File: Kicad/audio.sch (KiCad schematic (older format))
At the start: 33 parts, among them J15 AudioJack3, J16 AudioJack2, J17 AudioJack3, J18 AudioJack3, U15 TLV320AIC23BPW, Y3 12 MHz

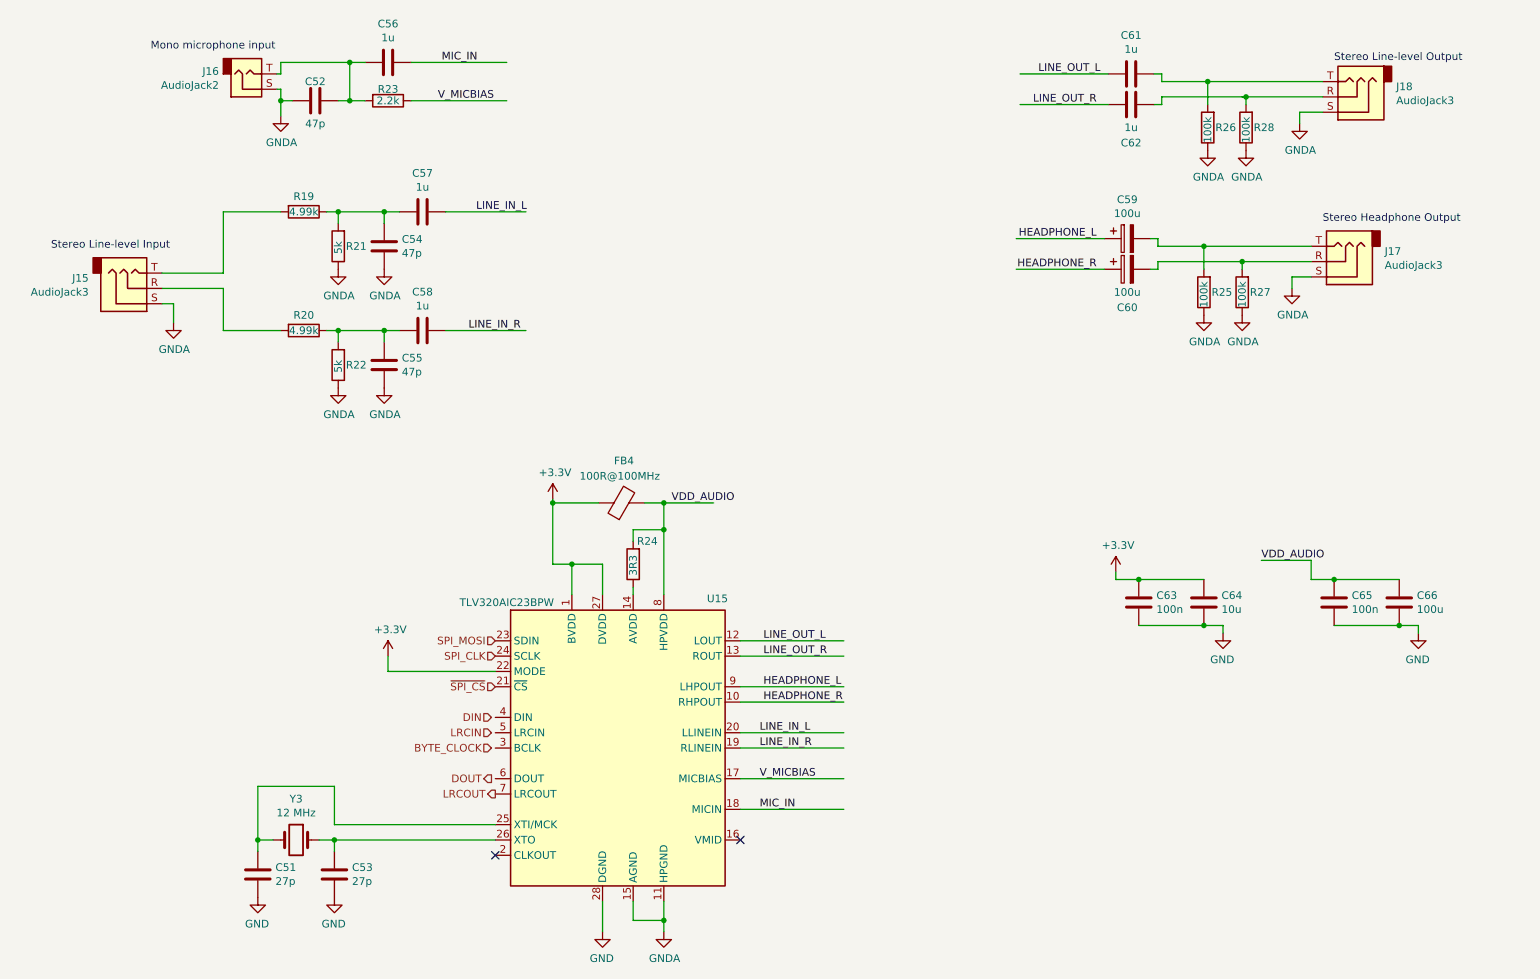
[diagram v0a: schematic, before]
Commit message: Removed USB FS hub. Added stacked USB A connector.
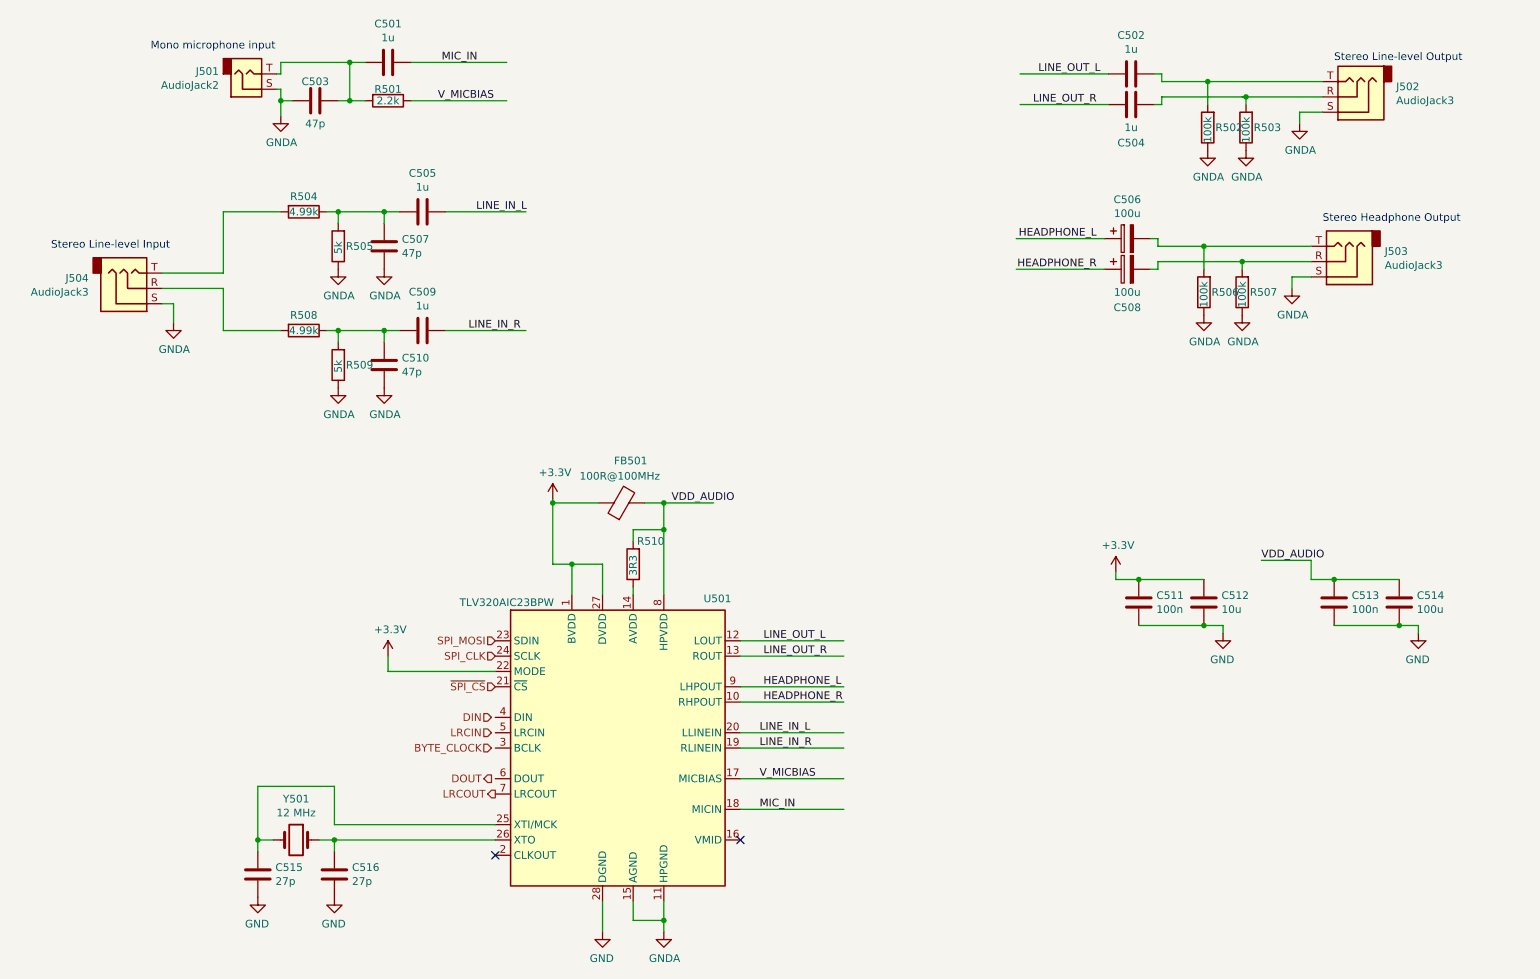
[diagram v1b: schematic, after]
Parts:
- C503: renamed from C52; footprint (none) -> Capacitor_SMD:C_0402_1005Metric
- C507: renamed from C54; footprint (none) -> Capacitor_SMD:C_0402_1005Metric
- C510: renamed from C55; footprint (none) -> Capacitor_SMD:C_0402_1005Metric
- C515: renamed from C51; footprint (none) -> Capacitor_SMD:C_0402_1005Metric
- C516: renamed from C53; footprint (none) -> Capacitor_SMD:C_0402_1005Metric
- R501: renamed from R23; footprint (none) -> Resistor_SMD:R_0402_1005Metric
- R502: renamed from R26; footprint (none) -> Resistor_SMD:R_0402_1005Metric
- R503: renamed from R28; footprint (none) -> Resistor_SMD:R_0402_1005Metric
- R504: renamed from R19; footprint (none) -> Resistor_SMD:R_0402_1005Metric
- R505: renamed from R21; footprint (none) -> Resistor_SMD:R_0402_1005Metric
- R506: renamed from R25; footprint (none) -> Resistor_SMD:R_0402_1005Metric
- R507: renamed from R27; footprint (none) -> Resistor_SMD:R_0402_1005Metric
- R508: renamed from R20; footprint (none) -> Resistor_SMD:R_0402_1005Metric
- R509: renamed from R22; footprint (none) -> Resistor_SMD:R_0402_1005Metric
- R510: renamed from R24; footprint (none) -> Resistor_SMD:R_0402_1005Metric
- renumbered C56 to C501, C61 to C502, C62 to C504, C57 to C505, C59 to C506, C60 to C508, C58 to C509, C63 to C511, C64 to C512, C65 to C513, C66 to C514, FB4 to FB501, J16 to J501, J18 to J502, J17 to J503, J15 to J504, U15 to U501, Y3 to Y501

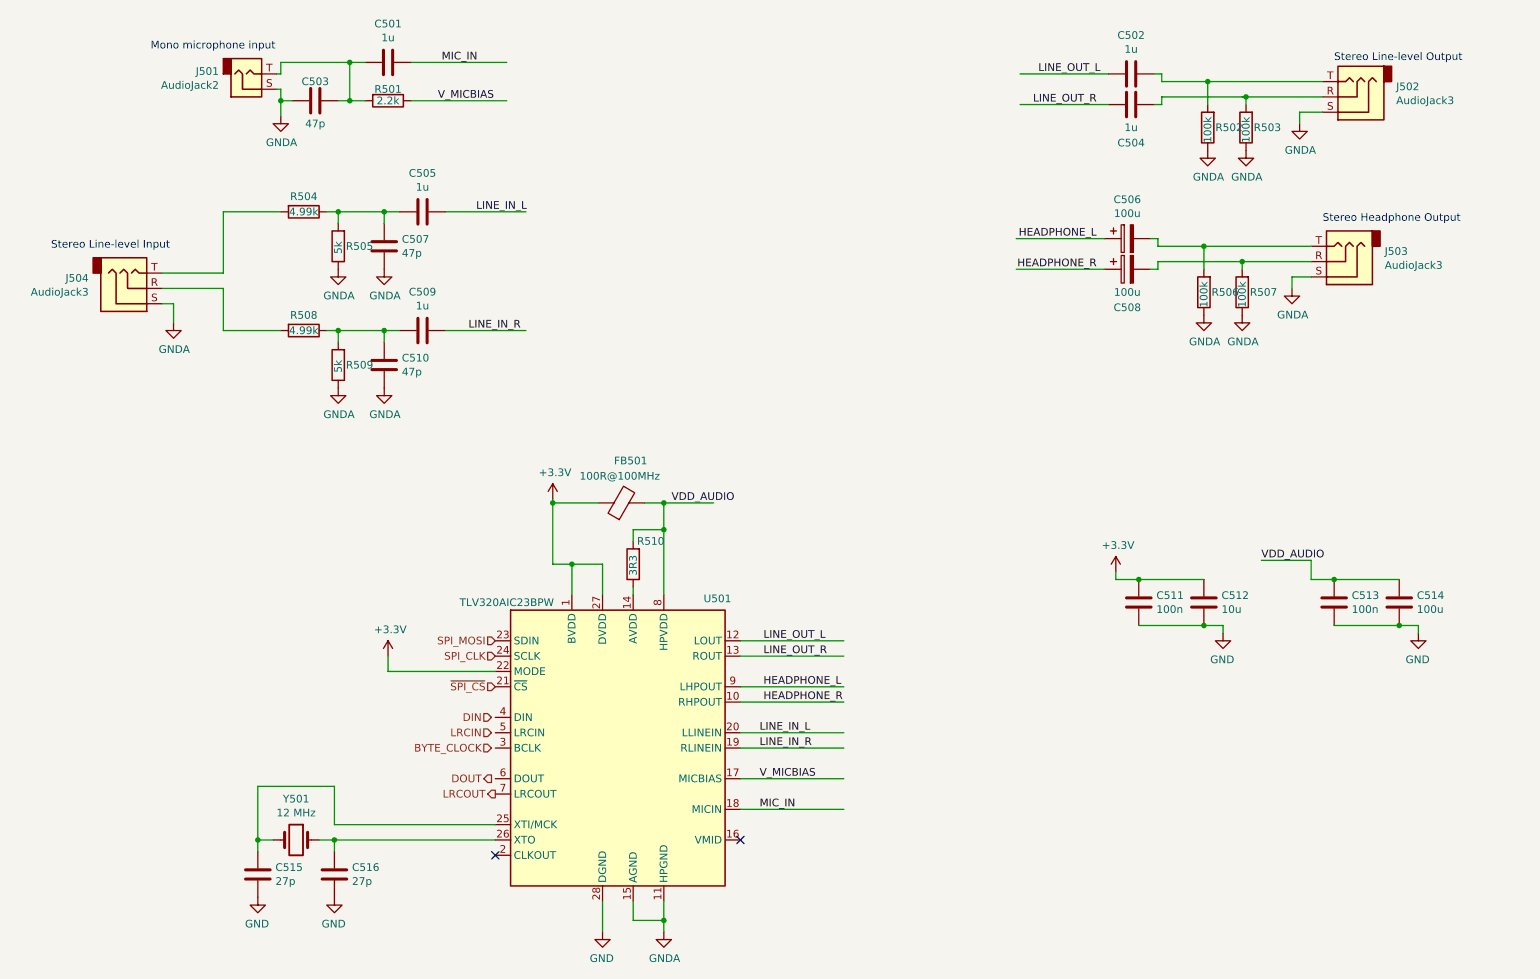
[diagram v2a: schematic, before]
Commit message: Tidying up schematic, and README.
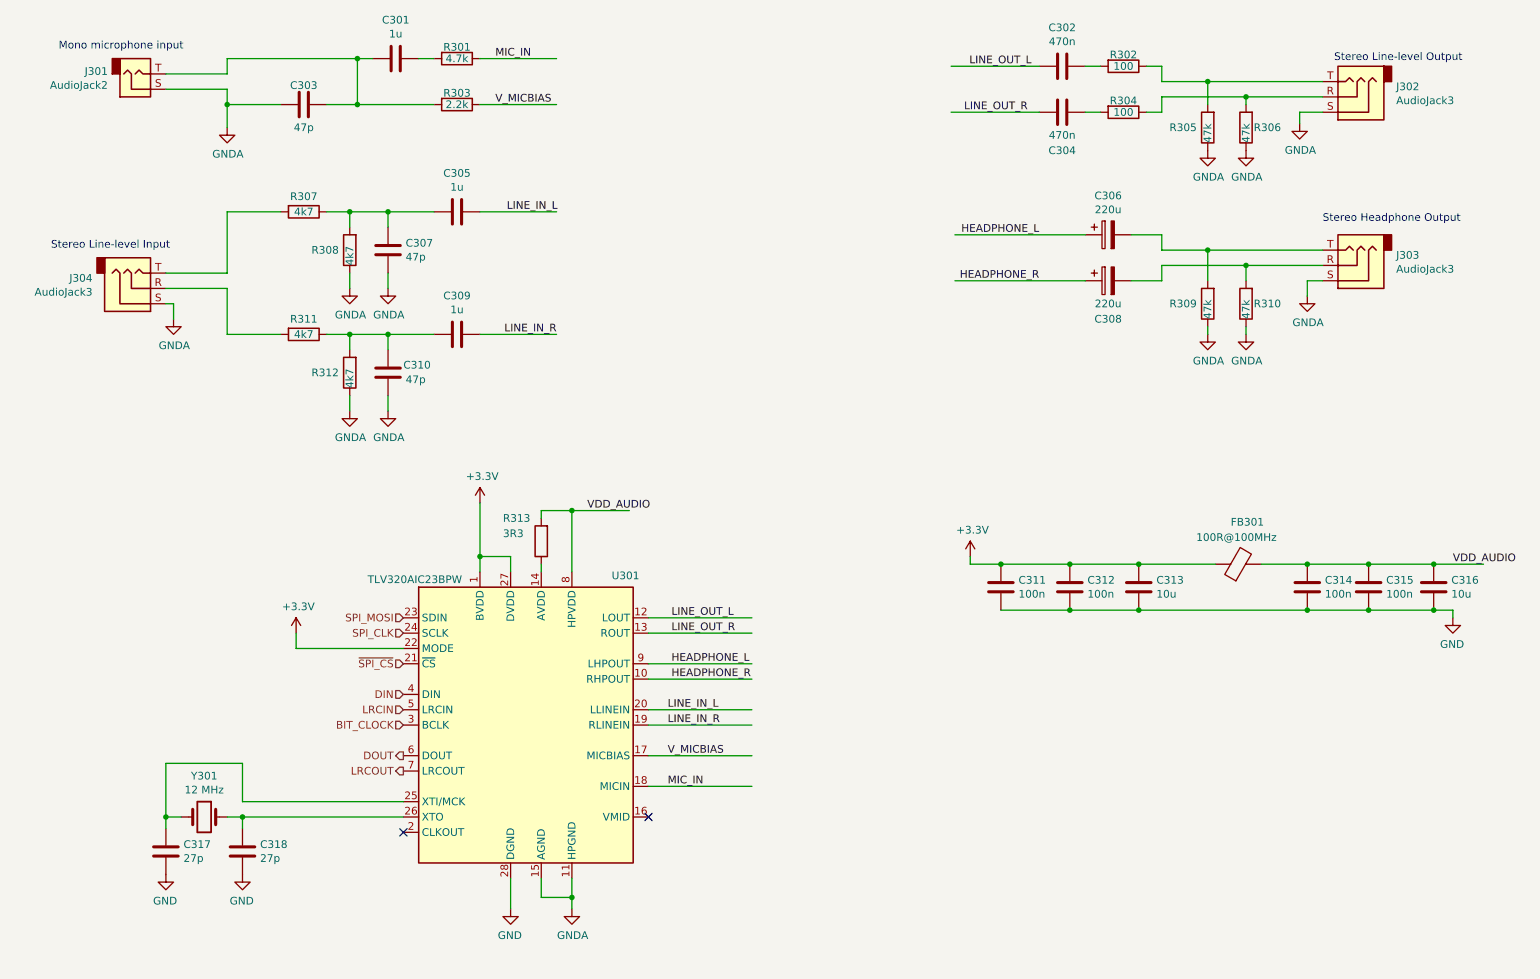
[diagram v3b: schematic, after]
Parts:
- removed C513: 100n, Capacitor_SMD:C_0402_1005Metric, symbol Device:C
- removed C514: 100u, Capacitor_Tantalum_SMD:CP_EIA-3528-21_Kemet-B, symbol Device:C
- added C312, C314, C315: 100n, Capacitor_SMD:C_0402_1005Metric, symbol Device:C
- added C316: 10u, Capacitor_SMD:C_0805_2012Metric, symbol Device:C
- added R301: 4.7k, Resistor_SMD:R_0402_1005Metric, symbol Device:R
- added R302, R304: 100, Resistor_SMD:R_0402_1005Metric, symbol Device:R
- C302: renamed from C502; value 1u -> 470n
- C304: renamed from C504; value 1u -> 470n
- C306: renamed from C506; value 100u -> 220u
- C308: renamed from C508; value 100u -> 220u
- R305: renamed from R502; value 100k -> 47k
- R306: renamed from R503; value 100k -> 47k
- R307: renamed from R504; value 4.99k -> 4k7
- R308: renamed from R505; value 5k -> 4k7
- R309: renamed from R506; value 100k -> 47k
- R310: renamed from R507; value 100k -> 47k
- R311: renamed from R508; value 4.99k -> 4k7
- R312: renamed from R509; value 5k -> 4k7
- renumbered C501 to C301, C503 to C303, C505 to C305, C507 to C307, C509 to C309, C510 to C310, C511 to C311, C512 to C313, C515 to C317, C516 to C318, FB501 to FB301, J501 to J301, J502 to J302, J503 to J303, J504 to J304, R501 to R303, R510 to R313, U501 to U301, Y501 to Y301
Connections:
- net labels added: BIT_CLOCK
- net labels removed: BYTE_CLOCK
- wire segments 113 -> 119
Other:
- moved on the sheet: C301, C302, C303, C304, C305, C306, C307, C308, C309, C310, C311, C313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
